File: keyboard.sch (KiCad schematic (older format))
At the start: 140 parts, among them J1 Conn_01x11, J2 Conn_01x11

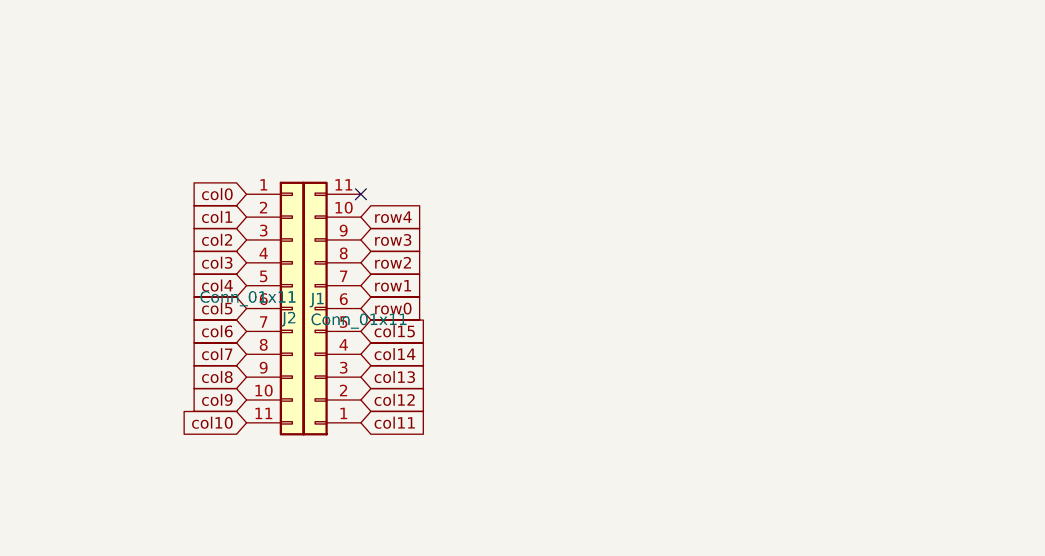
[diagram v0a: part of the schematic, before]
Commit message: Add Adafruit feather wing socket. Version 0.1
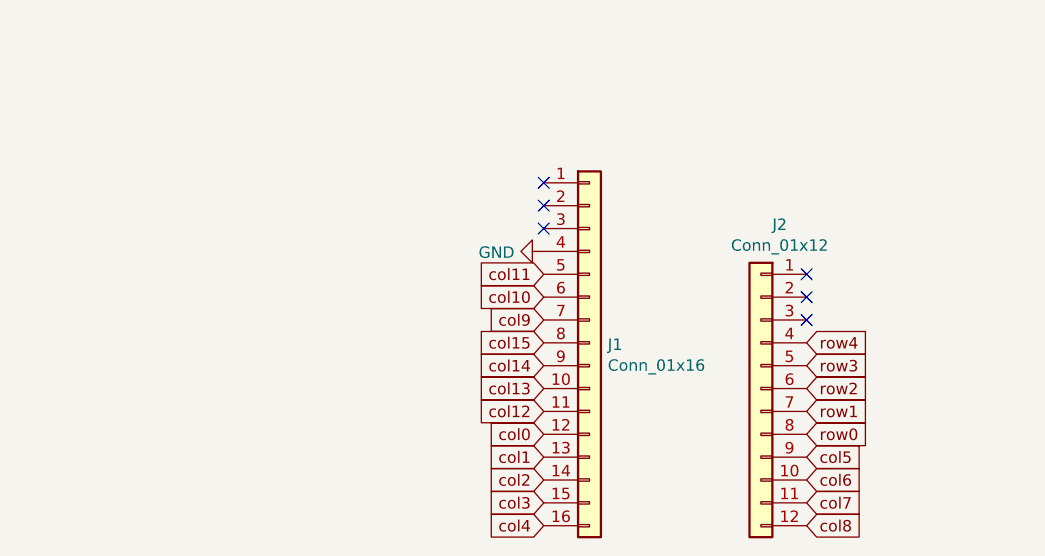
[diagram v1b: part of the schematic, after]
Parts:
- removed J1, J2: Conn_01x11, Connector_PinHeader_2.54mm:PinHeader_1x11_P2.54mm_Vertical, symbol Connector_Generic:Conn_01x11
- added J1: Conn_01x16, Connector_PinSocket_2.54mm:PinSocket_1x16_P2.54mm_Vertical, symbol Connector_Generic:Conn_01x16
- added J2: Conn_01x12, Connector_PinSocket_2.54mm:PinSocket_1x12_P2.54mm_Vertical, symbol Connector_Generic:Conn_01x12
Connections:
- net col0: now also J1.12 (Pin_12)
- net col1: now also J1.13 (Pin_13)
- net col10: now also J1.6 (Pin_6)
- net col11: now also J1.5 (Pin_5)
- net col12: now also J1.11 (Pin_11)
- net col13: now also J1.10 (Pin_10)
- net col14: now also J1.9 (Pin_9)
- net col15: now also J1.8 (Pin_8)
- net col2: now also J1.14 (Pin_14)
- net col3: now also J1.15 (Pin_15)
- net col4: now also J1.16 (Pin_16)
- net col5: now also J2.9 (Pin_9)
- net col6: now also J2.10 (Pin_10)
- net col7: now also J2.11 (Pin_11)
- net col8: now also J2.12 (Pin_12)
- net col9: now also J1.7 (Pin_7)
- net row0: now also J2.8 (Pin_8)
- net row1: now also J2.7 (Pin_7)
- net row2: now also J2.6 (Pin_6)
- net row3: now also J2.5 (Pin_5)
- net row4: now also J2.4 (Pin_4)
- new net GND: J1.4 (Pin_4)
- no-connect marks 1 -> 6
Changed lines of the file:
@@
 Wire Wire Line
 	16800 950  16800 1950
-Text GLabel 3500 6400 0    50   Input ~ 0
+$Comp
+L Connector_Generic:Conn_01x12 J2
+U 1 1 60201682
+P 5750 7250
+F 0 "J2" H 5668 7967 50  0000 C CNN
+F 1 "Conn_01x12" H 5668 7876 50  0000 C CNN
+F 2 "Connector_PinSocket_2.54mm:PinSocket_1x12_P2.54mm_Vertical" H 5750 7250 50  0001 C CNN
+F 3 "~" H 5750 7250 50  0001 C CNN
+	1    5750 7250
+	-1   0    0    -1
+$EndComp
+Text GLabel 4800 7450 0    50   Input ~ 0
 col0
-Text GLabel 3500 6500 0    50   Input ~ 0
+Text GLabel 4800 7550 0    50   Input ~ 0
 col1
-Text GLabel 3500 6600 0    50   Input ~ 0
+Text GLabel 4800 7650 0    50   Input ~ 0
 col2
-Text GLabel 3500 6700 0    50   Input ~ 0
+Text GLabel 4800 7750 0    50   Input ~ 0
 col3
-Text GLabel 3500 6800 0    50   Input ~ 0
+Text GLabel 4800 7850 0    50   Input ~ 0
 col4
-Text GLabel 3500 6900 0    50   Input ~ 0
+Text GLabel 5950 7550 2    50   Input ~ 0
 col5
-Text GLabel 3500 7000 0    50   Input ~ 0
+Text GLabel 5950 7650 2    50   Input ~ 0
 col6
-Text GLabel 3500 7100 0    50   Input ~ 0
+Text GLabel 5950 7750 2    50   Input ~ 0
 col7
-Text GLabel 3500 7200 0    50   Input ~ 0
+Text GLabel 5950 7850 2    50   Input ~ 0
 col8
-Text GLabel 3500 7300 0    50   Input ~ 0
+Text GLabel 4800 6950 0    50   Input ~ 0
 col9
-Text GLabel 4000 7300 2    50   Input ~ 0
+Text GLabel 4800 6850 0    50   Input ~ 0
+col10
+Text GLabel 4800 6750 0    50   Input ~ 0
+col11
+Text GLabel 4800 7350 0    50   Input ~ 0
 col12
-Text GLabel 4000 7200 2    50   Input ~ 0
+Text GLabel 4800 7250 0    50   Input ~ 0
 col13
-Text GLabel 4000 7100 2    50   Input ~ 0
+Text GLabel 4800 7150 0    50   Input ~ 0
 col14
-Text GLabel 4000 7000 2    50   Input ~ 0
+Text GLabel 4800 7050 0    50   Input ~ 0
 col15
-Text GLabel 3500 7400 0    50   Input ~ 0
-col10
-Text GLabel 4000 7400 2    50   Input ~ 0
-col11
-Text GLabel 4000 6900 2    50   Input ~ 0
+Text GLabel 5950 7450 2    50   Input ~ 0
 row0
-Text GLabel 4000 6800 2    50   Input ~ 0
+Text GLabel 5950 7350 2    50   Input ~ 0
 row1
-Text GLabel 4000 6700 2    50   Input ~ 0
+Text GLabel 5950 7250 2    50   Input ~ 0
 row2
-Text GLabel 4000 6600 2    50   Input ~ 0
+Text GLabel 5950 7150 2    50   Input ~ 0
 row3
-Text GLabel 4000 6500 2    50   Input ~ 0
+Text GLabel 5950 7050 2    50   Input ~ 0
 row4
-NoConn ~ 4000 6400
+NoConn ~ 5950 6950
+NoConn ~ 5950 6850
+NoConn ~ 5950 6750
+NoConn ~ 4800 6550
+NoConn ~ 4800 6450
+NoConn ~ 4800 6350
 $Comp
-L Connector_Generic:Conn_01x11 J1
-U 1 1 5FFB827D
-P 3700 6900
-F 0 "J1" H 3780 6942 50  0000 L CNN
-F 1 "Conn_01x11" H 3780 6851 50  0000 L CNN
-F 2 "Connector_PinHeader_2.54mm:PinHeader_1x11_P2.54mm_Vertical" H 3700 6900 50  0001 C CNN
-F 3 "~" H 3700 6900 50  0001 C CNN
-	1    3700 6900
+L Connector_Generic:Conn_01x16 J1
+U 1 1 60207F78
+P 5000 7050
+F 0 "J1" H 5080 7042 50  0000 L CNN
+F 1 "Conn_01x16" H 5080 6951 50  0000 L CNN
+F 2 "Connector_PinSocket_2.54mm:PinSocket_1x16_P2.54mm_Vertical" H 5000 7050 50  0001 C CNN
+F 3 "~" H 5000 7050 50  0001 C CNN
+	1    5000 7050
 	1    0    0    -1
 $EndComp
 $Comp
-L Connector_Generic:Conn_01x11 J2
-U 1 1 5FFB9CED
-P 3800 6900
-F 0 "J2" H 3880 6942 50  0000 L CNN
-F 1 "Conn_01x11" H 3880 6851 50  0000 L CNN
-F 2 "Connector_PinHeader_2.54mm:PinHeader_1x11_P2.54mm_Vertical" H 3800 6900 50  0001 C CNN
-F 3 "~" H 3800 6900 50  0001 C CNN
-	1    3800 6900
-	-1   0    0    1
+L power:GND #PWR?
+U 1 1 602E6ACE
+P 4800 6650
+F 0 "#PWR?" H 4800 6400 50  0001 C CNN
+F 1 "GND" V 4805 6522 50  0000 R CNN
+F 2 "" H 4800 6650 50  0001 C CNN
+F 3 "" H 4800 6650 50  0001 C CNN
+	1    4800 6650
+	0    1    1    0
 $EndComp
 $EndSCHEMATC
